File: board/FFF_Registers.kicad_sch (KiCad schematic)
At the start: 20 parts, among them U41 74F573, U42 74F573, U43 74F573, U44 74F541, U45 74F541, U46 74F541, U47 74F08, U48 74F02, U49 74F573, U50 74F541

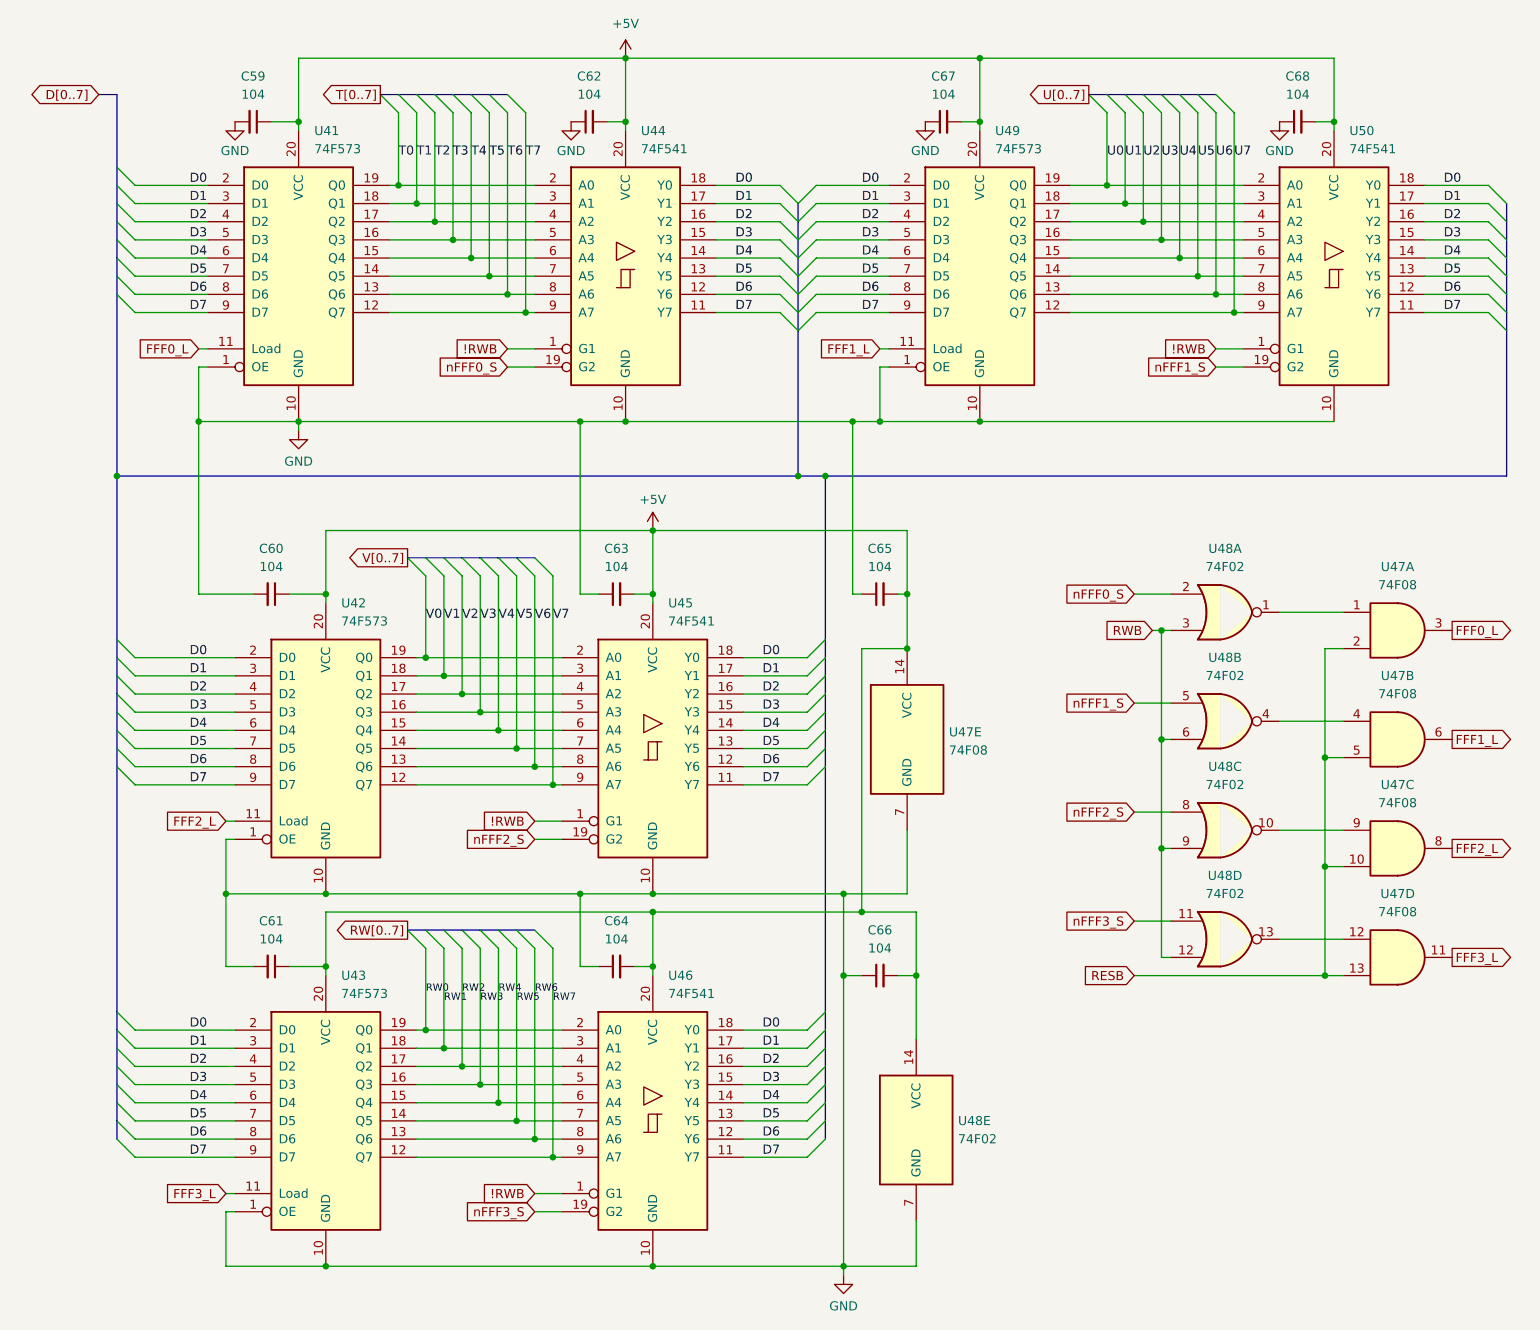
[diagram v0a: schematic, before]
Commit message: V2.0: wait states, GAL glue logic, serial clock and review fixes
Main board schematic:
- Replace the T4-T7 clock divider with RDY wait states. Fixed 7.16 MHz
  CPU clock; J36 selects 3.58 MHz for Rockwell parts. Waits are set per
  region through the write-only register at $FFF5 (reset = 3 waits).
- Move address decode, strobes, the wait-state generator, the IRQ
  encoder/latch/vector mux, ROM bank gating and DMA sync into seven GALs
  (U81-U86 ATF22V10C, U87 ATF16V8C), removing 29 ICs. CUPL sources,
  JEDECs and notes are in board/PLDs/V2.
- 1.8432 MHz serial clock, soft-power latch, -5V regulator, bulk caps,
  pull-ups, audio coupling/decoupling, GNDA tie, read-only Z register
  and other design-review fixes.
- New WaitStates and Support sheets; project symbol library
  hydra16.kicad_sym with sym-lib-table.

PCB updated from the schematic. Includes pending changes to the counter,
bus breakout and memory daughter card projects.

Firmware:
- Remove S_REGISTER; T/U/V/W now at $FFF0-$FFF3 to match the hardware.
- Add math.s and sound.s (included by os_main.s).
- Rebuild the 65C02 ROM image.

Co-Authored-By: Claude Opus 5.5 <noreply@anthropic.com>
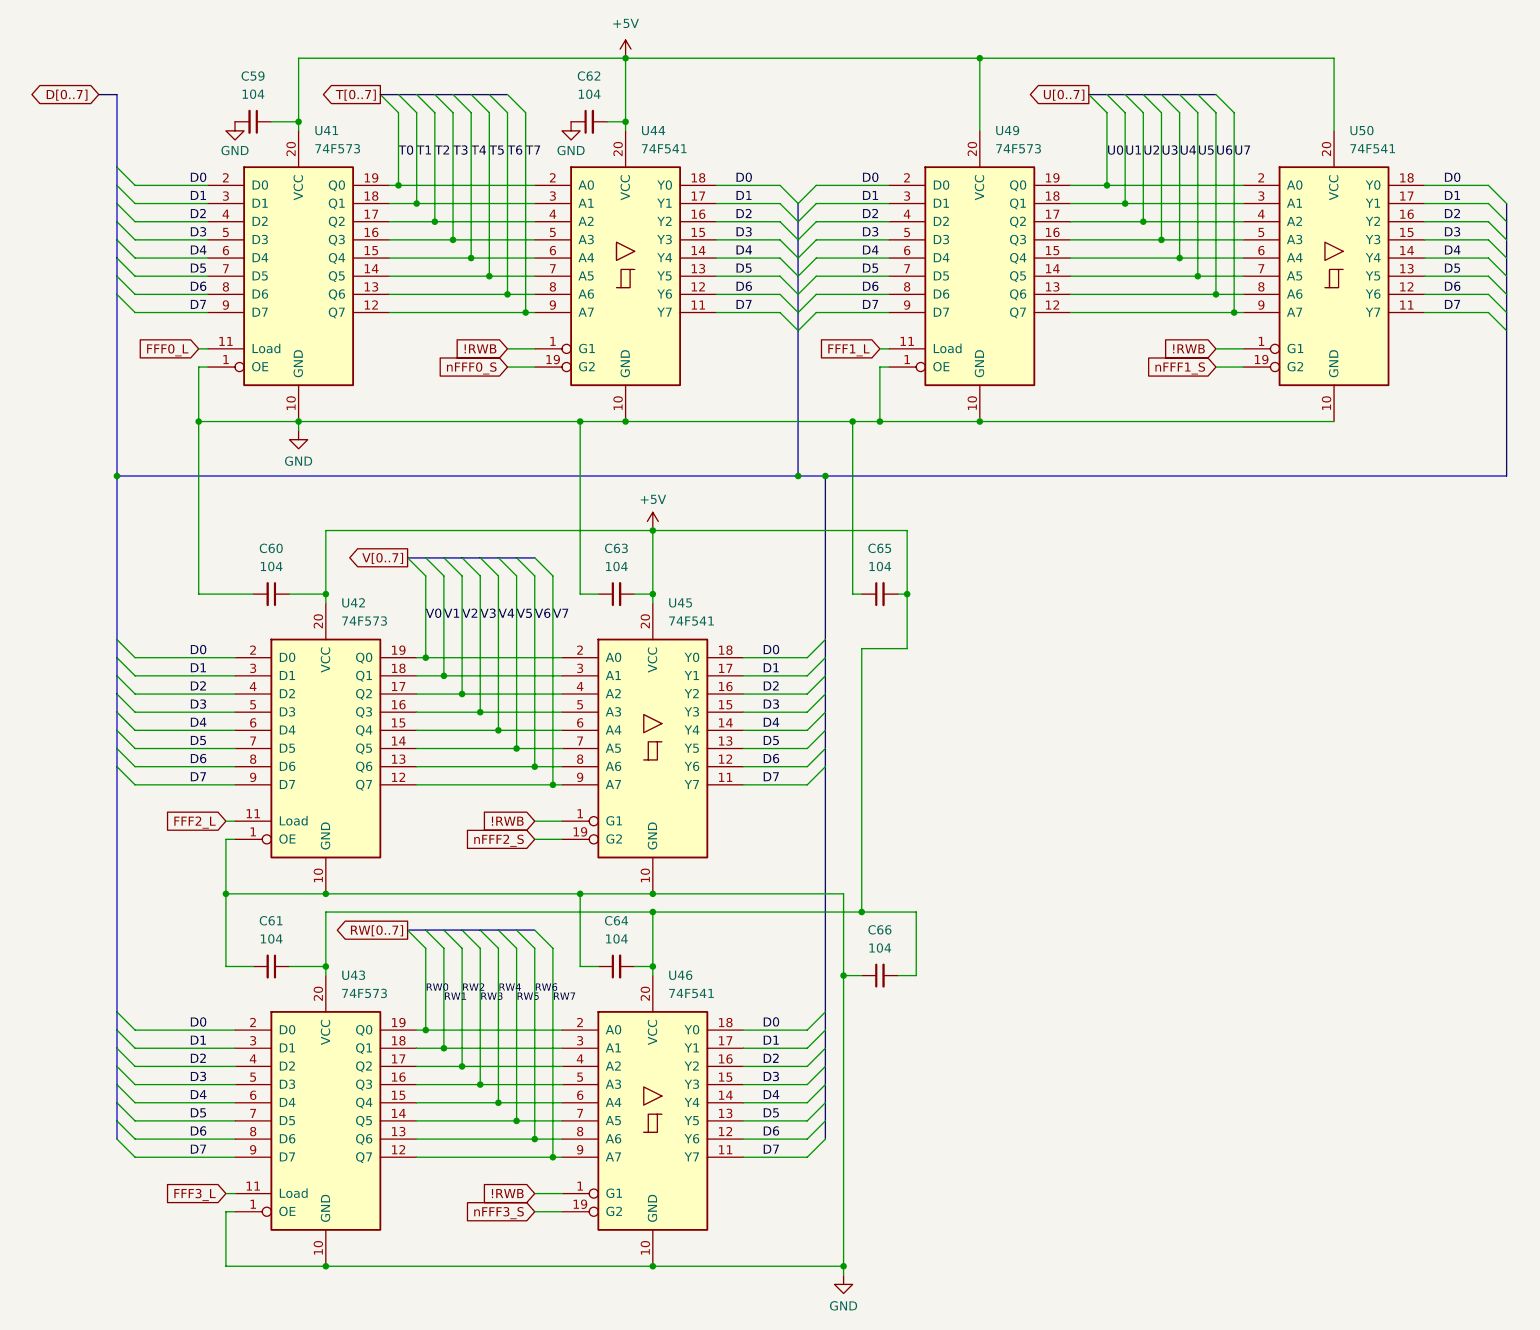
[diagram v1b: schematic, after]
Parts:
- removed C67, C68: 104, Capacitor_THT:C_Disc_D5.0mm_W2.5mm_P5.00mm, symbol Device:C_Small
- removed U47: 74F08, Package_DIP:DIP-14_W7.62mm_Socket_LongPads, symbol 74xx:74LS08
- removed U48: 74F02, Package_DIP:DIP-14_W7.62mm_Socket_LongPads, symbol 74xx:74LS02

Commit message: V2.0 rev 2.0D: clock stretching, OS ROM paging and review fixes
Bus timing:
- New GAL C (U88) generates PHI2/PHI1 and the 3.58 MHz sound clock from
  the 14.318 MHz master, replacing the U35 74F191 divider. J36 now selects
  7.16 or 3.58 MHz.
- Banked RAM, banked ROM and slot I/O ($FF20-$FFEF) get one extra PHI2-low
  period plus 0-3 extra PHI2-high periods set in $FFF5 (GAL D). This
  replaces the on-board RDY wait generator; cards can still pull RDY.
- Write strobes are now hold-time safe: PHI1 comes straight from GAL C
  and RWB_M straight from GAL B2.

Review fixes:
- OS ROM chip enable from a single-level decode, output enable from
  GAL B1; -55 part specified. Full 4K OS ROM paging via GAL G.
- Vector RAM writes only during PHI2; $FFF0-$FFFF no longer slowed.
- YM2151 /WR on RWB_M. U62 removed. RB0-RB7 pull-ups (RN5).
- Slot clocks driven through U56 and U34 with 33R series resistors.
- J38 enables in-system flashing of the banked ROMs.
- W65C22S/W65C51N, AS6C4008, DS1813-5 and CY7C192-25 values; R4 1k.
- J7 pin 8 no longer +5V; +5VA renamed +5VSB; serial handshake loop.
- Sheet titles and revisions, slot symbol pin fixes, and project symbol
  and footprint libraries so the project opens on another machine.

Co-Authored-By: Claude Opus 5.5 <noreply@anthropic.com>
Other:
- title: ZeroPage $00/$01 Mirror Memory and RAM/ROM Bank Logic -> T / U / V / RW Registers ($FFF0-$FFF3)
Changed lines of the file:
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@@
 	(paper "USLetter")
 	(title_block
-		(title "ZeroPage $00/$01 Mirror Memory and RAM/ROM Bank Logic")
-		(date "2026-01-28")
-		(rev "2.0B")
+		(title "T / U / V / RW Registers ($FFF0-$FFF3)")
+		(date "2026-10-06")
+		(rev "2.0D")
 		(company "Data Tuning")
 		(comment 1 "Hydra 16")

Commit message: V2.0: speaker headers, A/D bus fix, layout edits
- On-board speakers LS1/LS2 replaced by 2-pin headers J40 (SPEAKER L)
  and J41 (SPEAKER R) for external mini speakers: pin 1 speaker
  (through R30/R31), pin 2 GNDA; J18 still mutes them
- Connectors: a layout move had joined the A[0..15] and D[0..7] buses
  at two crossings (shorting A0-A7 to D0-D7); buses separated again,
  connectivity matches the previous commit
- Layout edits across the sheets (no other connectivity change)
- PCB updated from the schematic

Co-Authored-By: Claude Opus 5.5 <noreply@anthropic.com>
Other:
- title: T / U / V / RW Registers ($FFF0-$FFF3) -> Expansion Slots, SPI Headers and Port A
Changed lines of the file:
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@@
 	(paper "USLetter")
 	(title_block
-		(title "T / U / V / RW Registers ($FFF0-$FFF3)")
+		(title "Expansion Slots, SPI Headers and Port A")
 		(date "2026-10-06")
 		(rev "2.0D")
